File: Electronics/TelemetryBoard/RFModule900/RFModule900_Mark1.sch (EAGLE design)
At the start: 166 parts, among them T1 DC08-73, T2 DC08-73, U1 TPS2561, U2 TPS2561, U3 LM75B, U4 LTC5505, U5 LTC5505, U6 MCP4728, U7 ADC128D818, U8 MIC5504-3.3YM5, U9 TCA9535, Y1 30 Mhz

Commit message: Fixed package on new IO expander
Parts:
- added D3: (no value), SparkFun-LED:LED0603
- added R44: 270, SparkFun-Resistors:RESISTOR0402
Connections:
- new net N$65: D3.A, U9.P00
- net PA_OVERTEMP_ALARM: now also D13.P$4, U$13.UART_RX, U9.P03
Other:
- moved on the sheet: C18, C48, C57, C58, C59, C60, C61, C62, C63, C64, D1, D2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

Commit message: Slight updates
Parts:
- removed SJ1, SJ3: JUMPER-PAD-3-2OF3_NC_BY_TRACE_SMALL, SparkFun-Passives:JUMPER-PAD-3-2OF3_NC_BY_TRACE_SMALL
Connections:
- removed net 3V1: SJ1.1, SJ3.1
- removed net N$19: C16.1, C49.+, R1.1, SJ1.2
- net GND: now also R44.1
- net N$4: now also D3.C, R44.2; no longer C2.1, C50.+, R2.1, SJ3.2
- net REFLECTED_POWER_REF: now also U6.VOUT_C; no longer U6.VOUT_A
- net VREG1_DAC: now also C16.1, C49.+, R1.1, U6.VOUT_A; no longer SJ1.3, U6.VOUT_B
- net VREG2_DAC: now also C2.1, C50.+, R2.1, U6.VOUT_B; no longer SJ3.3, U6.VOUT_C
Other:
- moved on the sheet: C63, U8

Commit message: Working on routing board
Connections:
- net TR_SWITCH_CTL: now also U$11.I
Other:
- note removed: "576-4310-1-ND"
- note removed: "576-4764-1-ND"
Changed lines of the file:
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@@
 <text x="91.44" y="279.4" size="1.4224" layer="97">I2C adress:</text>
 <text x="215.9" y="271.78" size="1.4224" layer="97">I2C adress:</text>
-<text x="-132.08" y="594.36" size="1.4224" layer="91">576-4310-1-ND</text>
-<text x="-132.08" y="591.82" size="1.4224" layer="91">576-4764-1-ND</text>
 <text x="-185.42" y="596.9" size="1.778" layer="91">Add switching supply to bring 12v to 3.6 lmz31704</text>
 <text x="-218.44" y="302.26" size="1.778" layer="97">R29 setting Vout to 3.6v</text>
@@
 <segment>
 <pinref part="GND39" gate="1" pin="GND"/>
-<wire x1="-50.8" y1="243.84" x2="-48.26" y2="243.84" width="0.1524" layer="91"/>
 <wire x1="-48.26" y1="243.84" x2="-45.72" y2="243.84" width="0.1524" layer="91"/>
 <wire x1="-45.72" y1="243.84" x2="-45.72" y2="241.3" width="0.1524" layer="91"/>
@@
 <wire x1="416.56" y1="22.86" x2="406.4" y2="22.86" width="0.1524" layer="91"/>
 <label x="406.4" y="22.86" size="1.27" layer="95" rot="R180" xref="yes"/>
+<pinref part="U$11" gate="G$1" pin="I"/>
 </segment>
 </net>
@@
 </segment>
 </net>
-<net name="N$51" class="0">
-<segment>
-<wire x1="-136.906" y1="595.122" x2="-132.334" y2="595.122" width="0.1524" layer="91"/>
-<wire x1="-132.334" y1="595.122" x2="-132.334" y2="590.55" width="0.1524" layer="91"/>
-<wire x1="-132.334" y1="590.55" x2="-117.856" y2="590.55" width="0.1524" layer="91"/>
-<wire x1="-117.856" y1="590.55" x2="-117.856" y2="596.392" width="0.1524" layer="91"/>
-<wire x1="-117.856" y1="596.392" x2="-132.334" y2="596.392" width="0.1524" layer="91"/>
-<wire x1="-132.334" y1="596.392" x2="-132.334" y2="595.122" width="0.1524" layer="91"/>
-</segment>
-</net>
 <net name="N$54" class="0">
 <segment>
@@
 <pinref part="U6" gate="G$1" pin="LDAC"/>
 <wire x1="203.2" y1="246.38" x2="198.12" y2="246.38" width="0.1524" layer="91"/>
-<wire x1="193.04" y1="246.38" x2="198.12" y2="246.38" width="0.1524" layer="91"/>
 <pinref part="R39" gate="G$1" pin="2"/>
 </segment>

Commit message: Routing analog sections
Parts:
- R1, R10, R11, R12, R13, R14, R15, R16, R17, R18, R19, R2, R20, R21, R22, R23, R24, R25, R26, R27, R28, R29, R3, R30, R31, R32, R33, R34, R35, R36, R37, R38, R39, R4, R40, R41, R42, R43, R44, R5, R6, R7, R8, R9: device SparkFun-Resistors:RESISTOR0402 -> SparkFun-Resistors:RESISTOR0402-RES

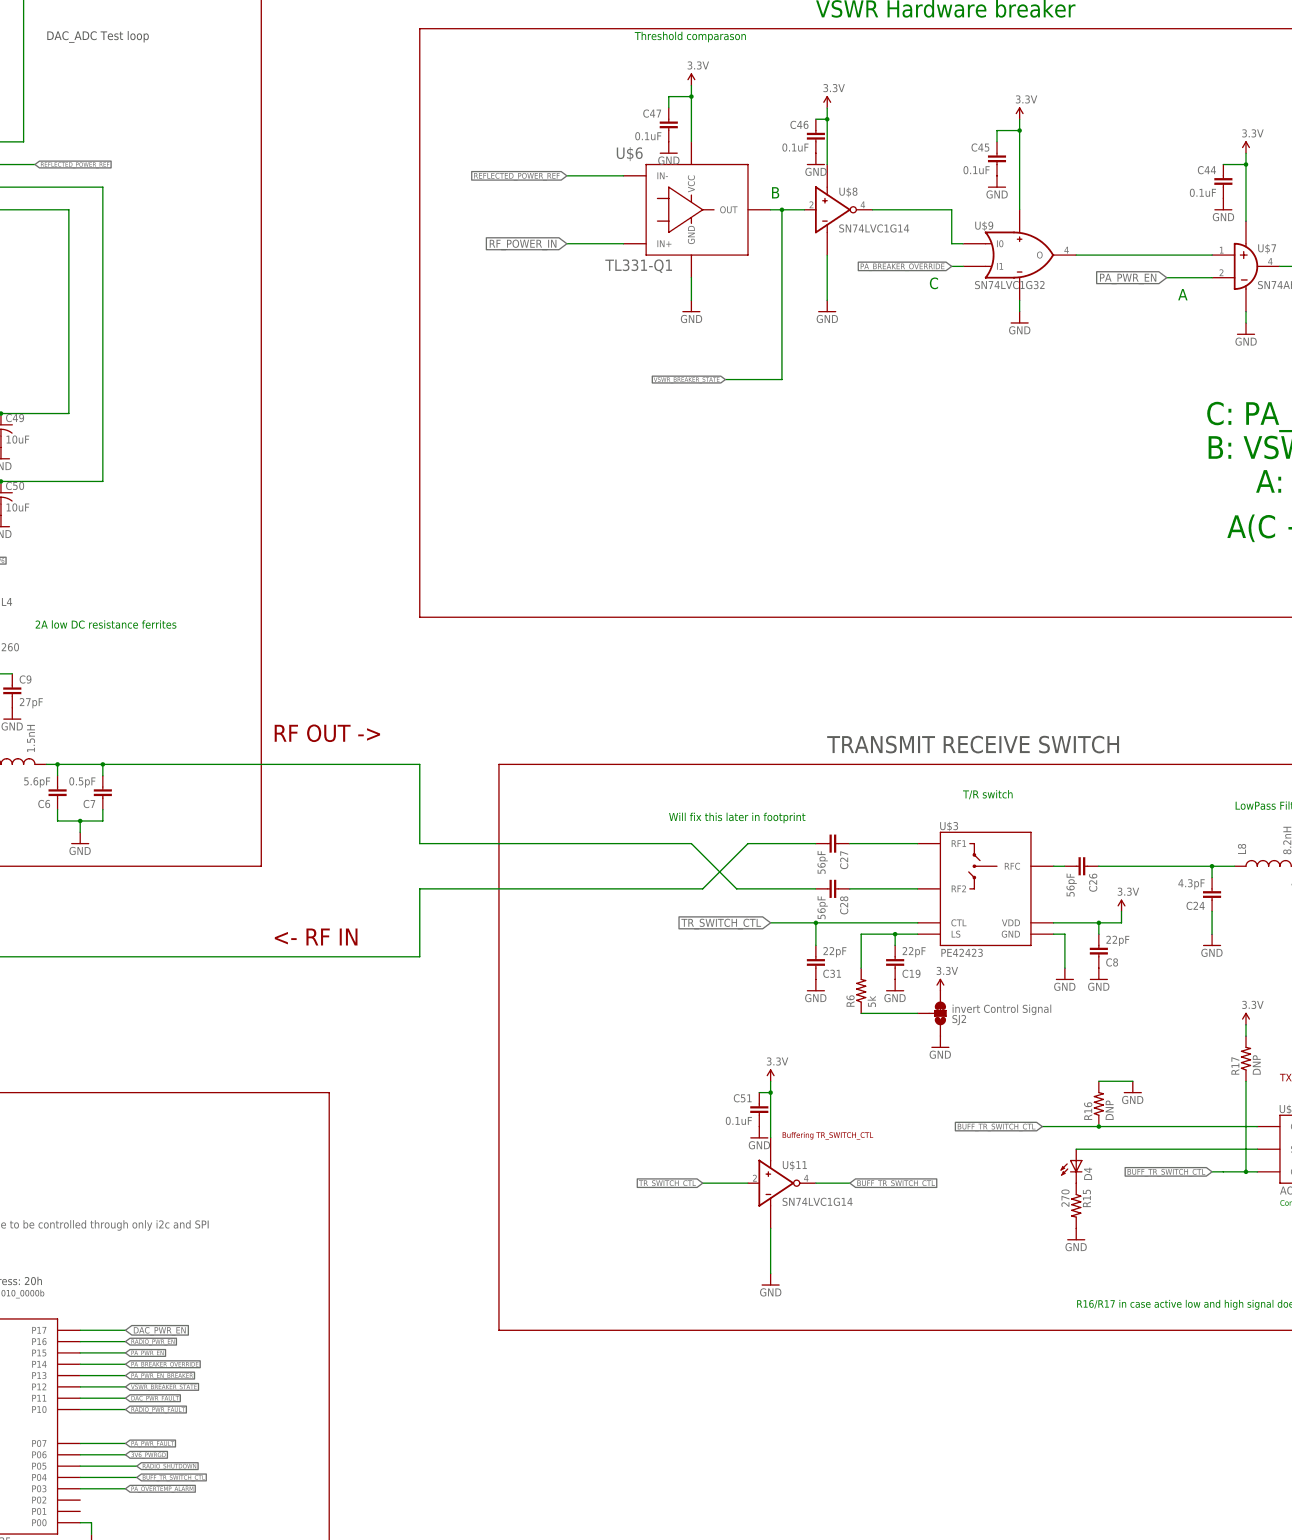
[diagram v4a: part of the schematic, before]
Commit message: Work in progress routing PSU
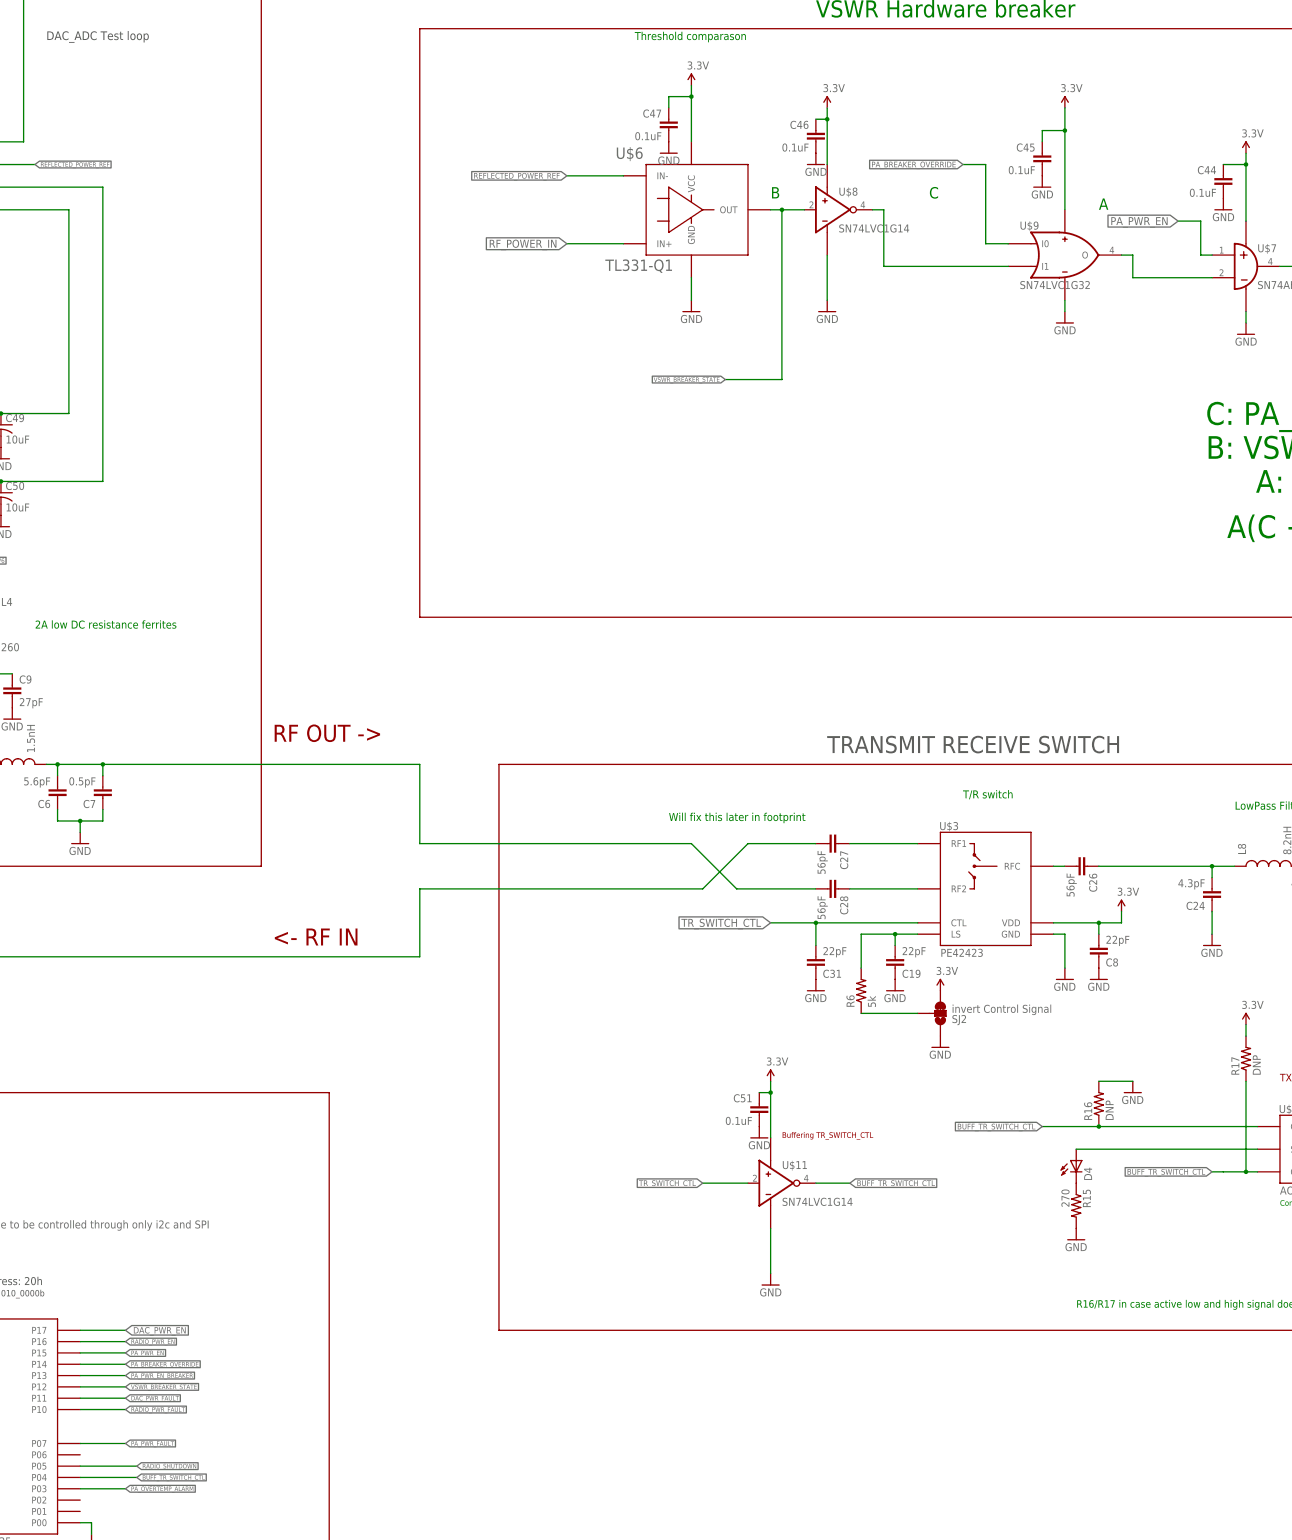
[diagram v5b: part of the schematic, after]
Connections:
- removed net N$38: U$8.O, U$9.I0
- removed net N$46: U$7.I0, U$9.O
- new net N$19: U$7.I1, U$9.O
- new net N$3: U$8.O, U$9.I1
- net 3V6_PWRGD: no longer U9.P06
- net PA_BREAKER_OVERRIDE: now also U$9.I0; no longer U$9.I1
- net PA_PWR_EN: now also U$7.I0; no longer U$7.I1
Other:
- moved on the sheet: C45, U$9
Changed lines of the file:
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@@
 <text x="391.16" y="279.4" size="1.778" layer="91">Threshold comparason</text>
 <text x="-185.42" y="612.14" size="1.778" layer="91">Add Temp sensor LM75B</text>
-<text x="457.2" y="223.52" size="2.54" layer="91">C</text>
 <text x="421.64" y="243.84" size="2.54" layer="91">B</text>
-<text x="513.08" y="220.98" size="2.54" layer="91">A</text>
 <text x="535.94" y="17.78" size="1.27" layer="91">Complementary Fet array</text>
 <text x="490.22" y="-5.08" size="1.6764" layer="91">R16/R17 in case active low and high signal does not turn off the complementary fets</text>
@@
 <wire x1="-20.32" y1="-114.3" x2="322.58" y2="-114.3" width="0.1524" layer="94"/>
 <wire x1="322.58" y1="-114.3" x2="322.58" y2="43.18" width="0.1524" layer="94"/>
+<text x="457.2" y="243.84" size="2.54" layer="91">C</text>
+<text x="495.3" y="241.3" size="2.54" layer="91">A</text>
 </plain>
 <instances>
@@
 <instance part="U$7" gate="G$1" x="528.32" y="228.6"/>
 <instance part="U$8" gate="G$1" x="434.34" y="241.3"/>
-<instance part="U$9" gate="G$1" x="477.52" y="231.14"/>
+<instance part="U$9" gate="G$1" x="487.68" y="231.14"/>
 <instance part="C38" gate="G$1" x="701.04" y="55.88"/>
 <instance part="GND48" gate="1" x="662.94" y="50.8"/>
@@
 <instance part="GND72" gate="1" x="241.3" y="266.7" rot="R180"/>
 <instance part="GND58" gate="1" x="434.34" y="218.44" rot="MR0"/>
-<instance part="GND59" gate="1" x="477.52" y="215.9" rot="MR0"/>
+<instance part="GND59" gate="1" x="487.68" y="215.9" rot="MR0"/>
 <instance part="GND60" gate="1" x="528.32" y="213.36" rot="MR0"/>
 <instance part="C44" gate="G$1" x="523.24" y="246.38" rot="MR0"/>
 <instance part="SUPPLY16" gate="G$1" x="528.32" y="254"/>
 <instance part="GND61" gate="1" x="523.24" y="241.3" rot="MR0"/>
-<instance part="SUPPLY17" gate="G$1" x="477.52" y="261.62"/>
+<instance part="SUPPLY17" gate="G$1" x="487.68" y="264.16"/>
 <instance part="SUPPLY18" gate="G$1" x="434.34" y="264.16"/>
 <instance part="SUPPLY20" gate="G$1" x="403.86" y="269.24"/>
-<instance part="C45" gate="G$1" x="472.44" y="251.46" rot="MR0"/>
+<instance part="C45" gate="G$1" x="482.6" y="251.46" rot="MR0"/>
 <instance part="C46" gate="G$1" x="431.8" y="256.54" rot="MR0"/>
 <instance part="C47" gate="G$1" x="398.78" y="259.08" rot="MR0"/>
 <instance part="GND65" gate="1" x="398.78" y="254" rot="MR0"/>
 <instance part="GND67" gate="1" x="431.8" y="251.46" rot="MR0"/>
-<instance part="GND68" gate="1" x="472.44" y="246.38" rot="MR0"/>
+<instance part="GND68" gate="1" x="482.6" y="246.38" rot="MR0"/>
 <instance part="R22" gate="G$1" x="35.56" y="25.4" rot="R90"/>
 <instance part="R23" gate="G$1" x="40.64" y="20.32" rot="R90"/>
@@
 <pinref part="U$9" gate="G$1" pin="GND"/>
 <pinref part="GND59" gate="1" pin="GND"/>
-<wire x1="477.52" y1="218.44" x2="477.52" y2="220.98" width="0.1524" layer="91"/>
+<wire x1="487.68" y1="218.44" x2="487.68" y2="220.98" width="0.1524" layer="91"/>
 </segment>
 <segment>
@@
 <pinref part="SUPPLY17" gate="G$1" pin="3.3V"/>
 <pinref part="U$9" gate="G$1" pin="VCC"/>
-<wire x1="477.52" y1="261.62" x2="477.52" y2="259.08" width="0.1524" layer="91"/>
+<wire x1="487.68" y1="264.16" x2="487.68" y2="259.08" width="0.1524" layer="91"/>
 <pinref part="C45" gate="G$1" pin="1"/>
-<wire x1="477.52" y1="259.08" x2="477.52" y2="241.3" width="0.1524" layer="91"/>
-<wire x1="472.44" y1="256.54" x2="472.44" y2="259.08" width="0.1524" layer="91"/>
-<wire x1="472.44" y1="259.08" x2="477.52" y2="259.08" width="0.1524" layer="91"/>
-<junction x="477.52" y="259.08"/>
+<wire x1="487.68" y1="259.08" x2="487.68" y2="241.3" width="0.1524" layer="91"/>
+<wire x1="482.6" y1="256.54" x2="482.6" y2="259.08" width="0.1524" layer="91"/>
+<wire x1="482.6" y1="259.08" x2="487.68" y2="259.08" width="0.1524" layer="91"/>
+<junction x="487.68" y="259.08"/>
 </segment>
 <segment>
@@
 <net name="PA_PWR_EN" class="0">
 <segment>
-<pinref part="U$7" gate="G$1" pin="I1"/>
-<wire x1="520.7" y1="226.06" x2="510.54" y2="226.06" width="0.1524" layer="91"/>
-<label x="510.54" y="226.06" size="1.778" layer="95" rot="R180" xref="yes"/>
-</segment>
-<segment>
 <wire x1="15.24" y1="-15.24" x2="7.62" y2="-15.24" width="0.1524" layer="91"/>
 <label x="7.62" y="-15.24" size="1.016" layer="95" rot="R180" xref="yes"/>
@@
 <label x="276.86" y="-15.24" size="1.016" layer="95" xref="yes"/>
 <pinref part="U9" gate="G$1" pin="P15"/>
+</segment>
+<segment>
+<wire x1="518.16" y1="238.76" x2="513.08" y2="238.76" width="0.1524" layer="91"/>
+<label x="513.08" y="238.76" size="1.778" layer="95" rot="R180" xref="yes"/>
+<wire x1="518.16" y1="238.76" x2="518.16" y2="231.14" width="0.1524" layer="91"/>
+<pinref part="U$7" gate="G$1" pin="I0"/>
+<wire x1="518.16" y1="231.14" x2="520.7" y2="231.14" width="0.1524" layer="91"/>
 </segment>
 </net>
@@
 </segment>
 </net>
-<net name="N$38" class="0">
-<segment>
-<pinref part="U$9" gate="G$1" pin="I0"/>
-<wire x1="464.82" y1="233.68" x2="462.28" y2="233.68" width="0.1524" layer="91"/>
-<wire x1="462.28" y1="233.68" x2="462.28" y2="241.3" width="0.1524" layer="91"/>
-<pinref part="U$8" gate="G$1" pin="O"/>
-<wire x1="462.28" y1="241.3" x2="444.5" y2="241.3" width="0.1524" layer="91"/>
-</segment>
-</net>
-<net name="N$46" class="0">
-<segment>
-<pinref part="U$7" gate="G$1" pin="I0"/>
-<pinref part="U$9" gate="G$1" pin="O"/>
-<wire x1="520.7" y1="231.14" x2="490.22" y2="231.14" width="0.1524" layer="91"/>
-</segment>
-</net>
 <net name="PA_BREAKER_OVERRIDE" class="0">
-<segment>
-<pinref part="U$9" gate="G$1" pin="I1"/>
-<wire x1="464.82" y1="228.6" x2="462.28" y2="228.6" width="0.1524" layer="91"/>
-<label x="462.28" y="228.6" size="1.27" layer="95" rot="R180" xref="yes"/>
-</segment>
 <segment>
 <wire x1="45.72" y1="-15.24" x2="53.34" y2="-15.24" width="0.1524" layer="91"/>
@@
 <label x="276.86" y="-17.78" size="1.016" layer="95" xref="yes"/>
 <pinref part="U9" gate="G$1" pin="P14"/>
+</segment>
+<segment>
+<label x="464.82" y="251.46" size="1.27" layer="95" rot="R180" xref="yes"/>
+<wire x1="464.82" y1="251.46" x2="469.9" y2="251.46" width="0.1524" layer="91"/>
+<wire x1="469.9" y1="251.46" x2="469.9" y2="233.68" width="0.1524" layer="91"/>
+<pinref part="U$9" gate="G$1" pin="I0"/>
+<wire x1="469.9" y1="233.68" x2="474.98" y2="233.68" width="0.1524" layer="91"/>
 </segment>
 </net>
@@
 <pinref part="U$13" gate="G$1" pin="DIFF_A+"/>
 </segment>
-<segment>
-<wire x1="276.86" y1="-38.1" x2="266.7" y2="-38.1" width="0.1524" layer="91"/>
-<label x="276.86" y="-38.1" size="1.016" layer="95" xref="yes"/>
-<pinref part="U9" gate="G$1" pin="P06"/>
-</segment>
 </net>
 <net name="N$56" class="0">
@@
 </segment>
 </net>
+<net name="N$3" class="0">
+<segment>
+<pinref part="U$8" gate="G$1" pin="O"/>
+<wire x1="444.5" y1="241.3" x2="447.04" y2="241.3" width="0.1524" layer="91"/>
+<wire x1="447.04" y1="241.3" x2="447.04" y2="228.6" width="0.1524" layer="91"/>
+<pinref part="U$9" gate="G$1" pin="I1"/>
+<wire x1="447.04" y1="228.6" x2="474.98" y2="228.6" width="0.1524" layer="91"/>
+</segment>
+</net>
+<net name="N$19" class="0">
+<segment>
+<pinref part="U$9" gate="G$1" pin="O"/>
+<wire x1="500.38" y1="231.14" x2="502.92" y2="231.14" width="0.1524" layer="91"/>
+<wire x1="502.92" y1="231.14" x2="502.92" y2="226.06" width="0.1524" layer="91"/>
+<pinref part="U$7" gate="G$1" pin="I1"/>
+<wire x1="502.92" y1="226.06" x2="520.7" y2="226.06" width="0.1524" layer="91"/>
+</segment>
+</net>
